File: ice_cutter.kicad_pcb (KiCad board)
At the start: 4 copper layers, 90 x 100 mm, 180 parts, among them J1 Conn_01x01_Male, J2 Barrel_Jack, J3 pot, J4 Conn_01x01_Male, J5 program, J6 program2, J7 hands, J8 UART, J9 xt60, M1 Motor_Servo, M2 Motor_Servo, Q1 Q_PMOS_GSD, Q10 S8050_SMD, Q11 Q_NMOS_GSD, Q12 Q_NMOS_GSD, Q13 Q_NMOS_GSD, Q14 Q_NMOS_GSD, Q15 S8550, Q16 S8050_SMD, Q17 S8050_SMD, Q18 S8050_SMD, Q2 Q_PMOS_GSD, Q3 Q_PMOS_GSD, Q4 S8550, Q5 Q_NMOS_GSD, Q6 S8550, Q7 Q_NMOS_GSD, Q8 S8050_SMD, Q9 S8050_SMD, SW1 SW_Push, SW2 SW_Push, SW3 SW_Push, U1 LM317_TO-252, U10 TMP117, U11 TM1620, U12 INA219AxD, U2 LM317_TO-252, U3 INA219AxD, U4 LM317_TO-252, U5 INA219AxD, U6 FJ4301AH, U7 FJ4301AH, U8 STM32G030XX, U9 SHT30-DIS

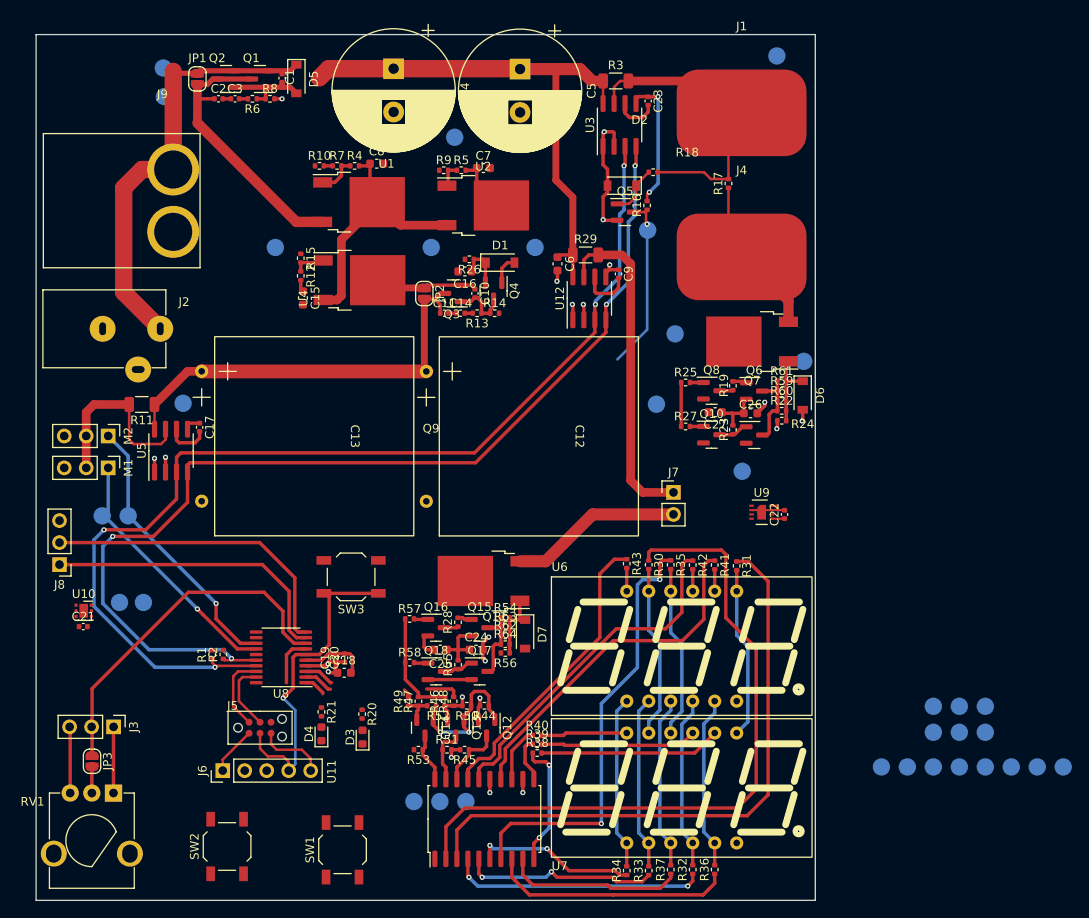
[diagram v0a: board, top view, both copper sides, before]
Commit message: got lazy, went 4 layer. Some of layer 3 done. progressing. Mainly committing for board chronological how to sake. Added Caps on the TM1620
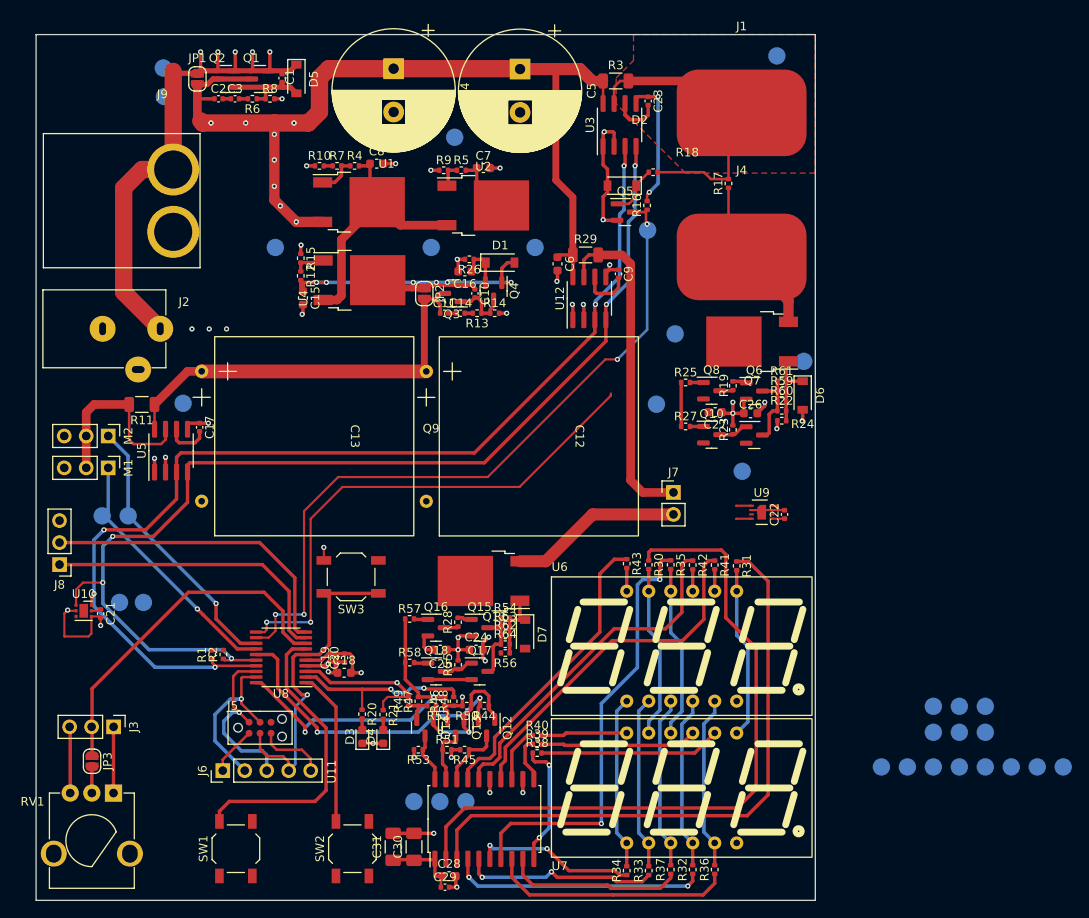
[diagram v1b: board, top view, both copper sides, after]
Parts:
- added C28: 10u, Capacitor_SMD:C_0603_1608Metric, F.Cu at (116.1, 126.6)
- added C29: 100n, Capacitor_SMD:C_0402_1005Metric, F.Cu at (115.6, 127.9)
- added C30: 100u, Capacitor_SMD:C_1206_3216Metric_Pad1.33x1.80mm_HandSolder, F.Cu at (112.0, 123.2)
- added C31: 100u, Capacitor_SMD:C_1206_3216Metric_Pad1.33x1.80mm_HandSolder, F.Cu at (109.6, 123.2)
- moved SW2 14.5 mm to (104.9, 123.4)
- moved SW1 12.3 mm to (91.4, 123.4)
- moved D4 7.14 mm to (108.5, 110.5)
- moved R21 7.14 mm to (108.5, 107.9)
- moved C21 2.50 mm to (75.8, 96.3), turned to -90 degrees
- moved D3 0.07 mm to (106.0, 110.5)
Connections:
- C11 pad 1: Net-(C11-Pad1) -> /5V_SS
- C12 pad 1: Net-(C11-Pad1) -> /5V_SS
- C13 pad 1: Net-(C11-Pad1) -> /5V_SS
- JP2 pad 2: Net-(C11-Pad1) -> /5V_SS
- M1 pad 2: /5V_SS -> /5V_SS_S
- M2 pad 2: /5V_SS -> /5V_SS_S
- Q3 pad 3: Net-(C11-Pad1) -> /5V_SS
- R11 pad 1: Net-(C11-Pad1) -> /5V_SS
- R11 pad 2: /5V_SS -> /5V_SS_S
- R45 pad 2: +5V -> /5V_SS
- R51 pad 2: +5V -> /5V_SS
- R53 pad 2: +5V -> /5V_SS
- U11 pad 1: +5V -> /5V_SS
- U5 pad 7: /5V_SS -> /5V_SS_S
- U5 pad 8: Net-(C11-Pad1) -> /5V_SS
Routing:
- net /VOUT_FAULT: track 20.5 -> 83.7 mm, vias 1 -> 4
- net /Drive_FET: track 5.08 -> 65.1 mm, vias 0 -> 2
- net Net-(C11-Pad1): track 48.8 -> 0.00 mm
- net /5V_SS: track 21.6 -> 60.7 mm, vias 0 -> 2
- net GND: track 83.0 -> 116.9 mm, vias 13 -> 28
- net /FROM_3V3: track 2.57 -> 36.0 mm, vias 1 -> 2
- net /PB1: track 5.73 -> 34.6 mm
- net +5V: track 18.6 -> 45.0 mm, vias 1 -> 6
- net /Hands: track 12.7 -> 37.9 mm, vias 0 -> 2
- net /5V_SS_S: track 0.00 -> 21.6 mm
- net +3V3: track 70.4 -> 89.2 mm, vias 9 -> 10
- net /PB2: track 2.56 -> 17.9 mm
- net /V_SS: track 95.1 -> 110.3 mm, vias 0 -> 8
- net /LED1: track 7.33 -> 21.2 mm, vias 0 -> 2
- net /LED2: track 4.53 -> 17.4 mm, vias 0 -> 1
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- added copper zone on In2.Cu, net /V_SS
- added copper zone on F.Cu, net /Wire_H
- added copper zone on In1.Cu, net GND
- added copper zone on In2.Cu, net VDC

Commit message: more PCB progress
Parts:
- moved U9 21.1 mm to (141.5, 66.3)
- moved C22 21.1 mm to (144.2, 66.6)
- moved TP31 14.7 mm to (88.4, 105.4), turned to 0 degrees
- moved TP30 11.5 mm to (85.6, 105.4), turned to 0 degrees
- moved TP26 8.11 mm to (140.1, 56.1)
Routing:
- net +12V: track 44.1 -> 149.2 mm, vias 4 -> 8
- net +3V3: track 89.2 -> 156.0 mm, vias 10 -> 20
- net GND: track 116.9 -> 174.6 mm, vias 28 -> 48
- net /SCL: track 129.6 -> 141.3 mm, vias 5 -> 7
- net /SDA: track 127.2 -> 137.2 mm, vias 5 -> 7
- net /Drive_FET: track 65.1 -> 73.1 mm, vias 2 -> 4
- net /PB2: track 17.9 -> 24.2 mm
- net /PB1: track 34.6 -> 40.9 mm
- net /5V_SS: track 60.7 -> 64.6 mm, vias 2 -> 12
- net /pot: track 40.9 -> 44.2 mm
- net /VOUT_FAULT: track 83.7 -> 82.8 mm
- added copper zone on In2.Cu, net +3V3
- added copper zone on In2.Cu, net /5V_SS

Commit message: finished v0 I hope
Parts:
- moved TP5 47.1 mm to (131.1, 114.4), turned to 90 degrees
- moved TP12 46.9 mm to (131.1, 104.9), turned to 90 degrees
- moved TP14 44.2 mm to (131.1, 101.9), turned to 90 degrees
- moved TP8 43.9 mm to (131.1, 111.4), turned to 90 degrees
- moved TP16 41.7 mm to (131.1, 98.9), turned to 90 degrees
- moved TP10 40.9 mm to (131.1, 108.4), turned to 90 degrees
- moved TP18 35.3 mm to (155.4, 98.4), turned to -90 degrees
- moved TP17 31.3 mm to (155.4, 101.4), turned to -90 degrees
- moved TP15 27.4 mm to (155.4, 104.4), turned to -90 degrees
- moved R41 25.2 mm to (126.6, 105.9), turned to 0 degrees
- moved TP13 23.6 mm to (155.4, 107.4), turned to -90 degrees
- moved R42 22.5 mm to (126.6, 104.7), turned to 0 degrees
- moved TP11 20.0 mm to (155.4, 110.4), turned to -90 degrees
- moved TP9 16.6 mm to (155.4, 113.4), turned to -90 degrees
- moved R43 16.3 mm to (126.6, 103.4), turned to 0 degrees
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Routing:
- net Net-(R41-Pad1): track 40.6 -> 11.6 mm
- net Net-(R42-Pad1): track 40.1 -> 14.9 mm
- net /Grid3: track 2.51 -> 26.9 mm, vias 0 -> 1
- net /A: track 20.0 -> 43.7 mm, vias 0 -> 2
- net /E: track 20.0 -> 41.5 mm, vias 0 -> 1
- net /Grid2: track 2.51 -> 23.7 mm, vias 0 -> 1
- net /D: track 20.0 -> 38.8 mm, vias 0 -> 2
- net /DP: track 20.0 -> 38.0 mm, vias 0 -> 1
- net Net-(R43-Pad1): track 34.6 -> 16.7 mm
- net /Grid1: track 2.67 -> 15.9 mm, vias 0 -> 1
- net /C: track 20.0 -> 33.2 mm, vias 0 -> 2
- net /F: track 20.0 -> 32.4 mm, vias 0 -> 2
- net /G: track 20.0 -> 32.1 mm, vias 0 -> 1
- net /B: track 19.9 -> 31.6 mm
- net /Wire_L: track 18.6 -> 28.3 mm, vias 0 -> 1
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- added copper zone on B.Cu, net GND
- added copper zone on F.Cu, net GND
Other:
- outline, holes or cut-outs redrawn
- board text added: "2022"
- board text added: "3V3"
- board text added: "5V"
- board text added: "5V_SS"
- board text added: "A"
- board text added: "CL"
- board text added: "CLK"
- board text added: "DA"
- board text added: "DP"
- board text added: "D_FET"
- board text added: "FET_GATE"
- board text added: "FROM"
- board text added: "G1"
- board text added: "G6"
- board text added: "GND"
- board text added: "Ice_Cutter"
- board text added: "M1"
- board text added: "M2"
- board text added: "STB"
- board text added: "V+"
- board text added: "V_FAULT"
- board text added: "V_SS"
- board text added: "Wire_H"
- board text added: "Wire_L"
- board text added: "v0.0"
